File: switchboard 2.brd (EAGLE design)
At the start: 100 x 65 mm, 217 parts, among them IC1 MT8816AP, IC10 Z8F2480SO, IC11 LMV321M5, IC12 74HC595D, IC14 74LVC1G125DBV, IC15 74LVC1G125DBV, IC16 LM2940-9, IC17 PC817S OPTO, IC2 NE5532D, IC3 TC7660-SOIC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

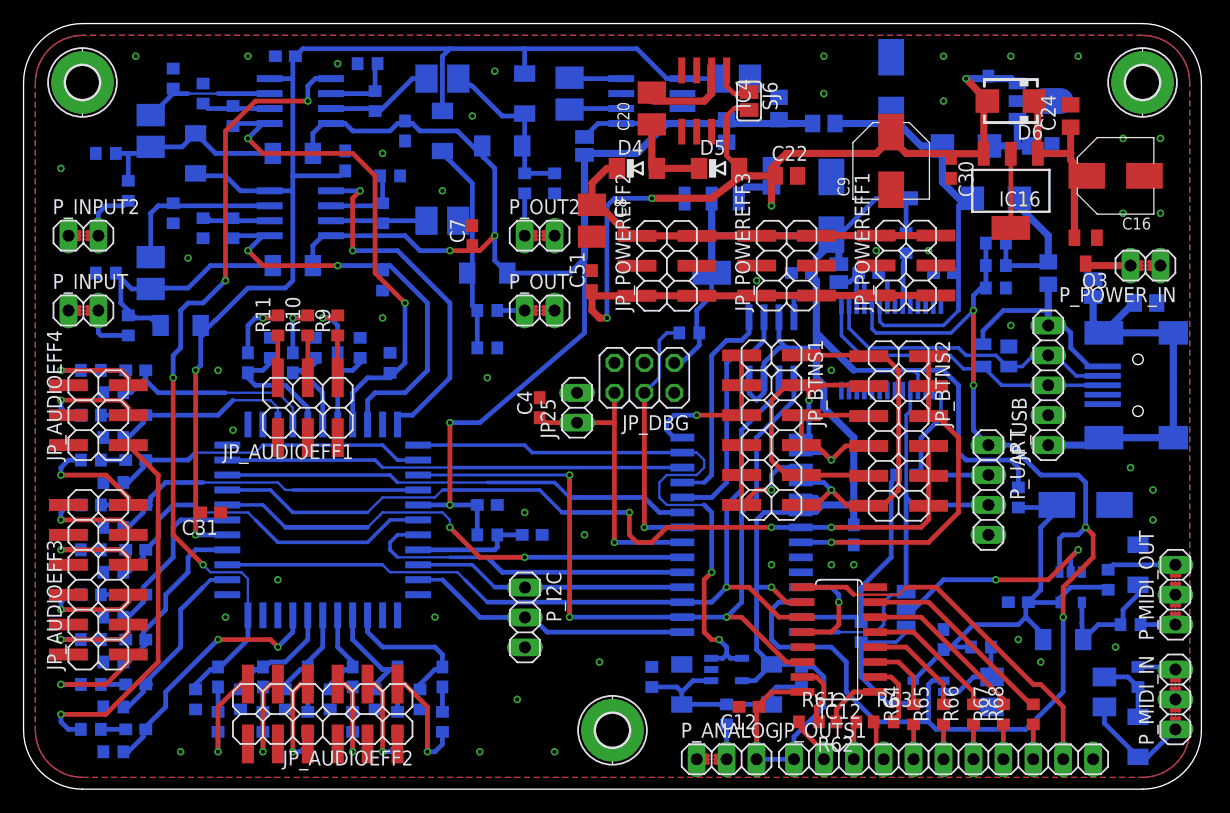
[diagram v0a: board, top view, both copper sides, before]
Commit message: Polarity inversion protection diode added to -5V. USB ESD protection connection changed from GND to USB shield. Layout development and changes to improve performance, considering current loops.
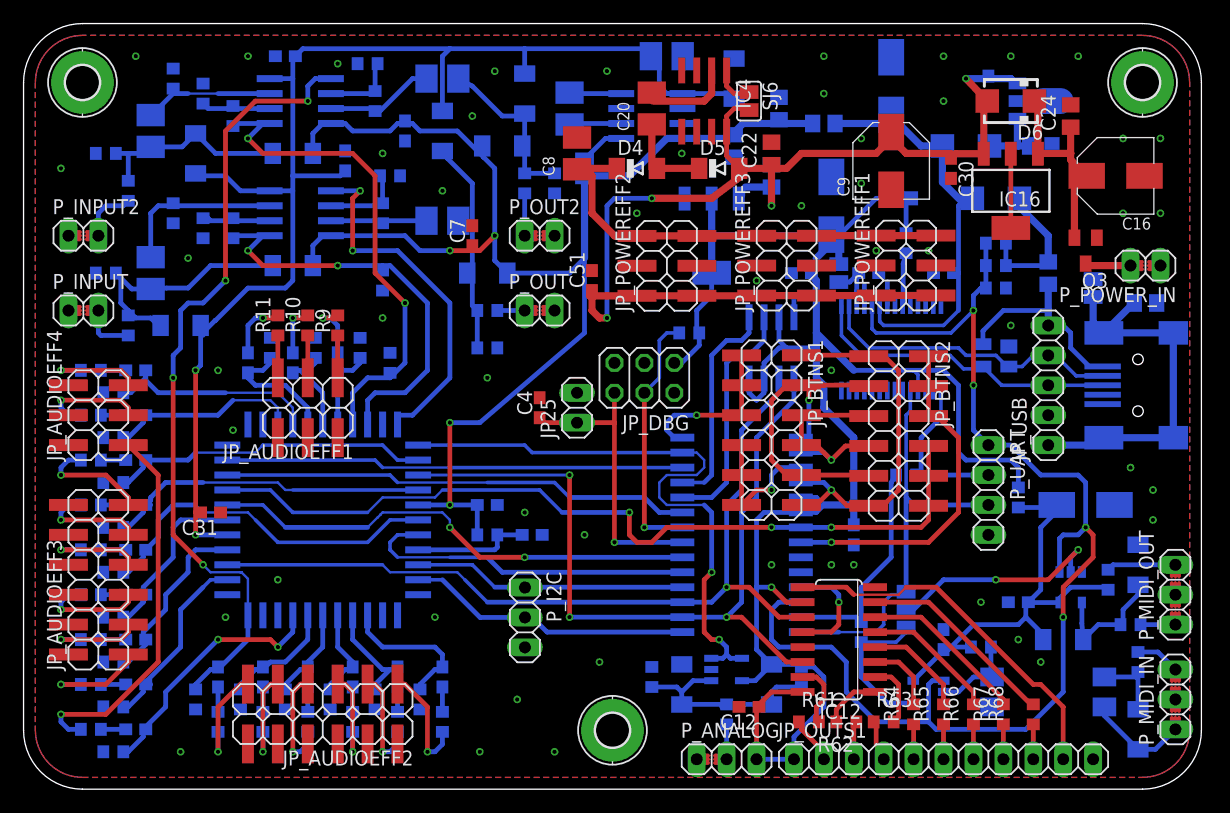
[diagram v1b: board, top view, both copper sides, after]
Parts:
- added D20: LL4148, diode:MINIMELF
- moved C19 6.02 mm to (54.6, 62.2)
- moved C8 5.85 mm to (47.0, 54.0), turned to 90 degrees
- moved C22 2.29 mm to (63.5, 54.0), turned to 90 degrees
- moved SJ1 1.91 mm to (47.6, 52.7)
- moved C25 1.42 mm to (60.3, 54.6)
- moved C5 1.27 mm to (46.4, 57.8)
- moved IC3 1.27 mm to (53.3, 57.1)
- moved R5 1.27 mm to (94.6, 10.8)
- moved D3 0.63 mm to (94.6, 5.08)
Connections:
- net -5V: now also D20.A
- net GND: now also D20.C, H1.B2,8, H2.B2,8, H3.B2,8; no longer D19.1
- net USB_SHLD: now also D19.1
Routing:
- net -5V: track 111.7 -> 115.9 mm
- net +18V: track 36.7 -> 40.6 mm
- net N$5: track 4.92 -> 3.85 mm
- net MIDI_IN2: track 11.1 -> 10.1 mm
- net MIDI_IN1: track 4.03 -> 4.86 mm
- net +9V: track 106.9 -> 107.6 mm
- net GND1: track 1.52 -> 2.16 mm
- net N$28: track 5.73 -> 6.27 mm
- net GND: vias 47 -> 53

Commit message: Final adjustments to the schematic and layout. Cap added close to the generic input opamp. RC filter against EMI added to the audio inputs. Bias resistors added to output opamps.
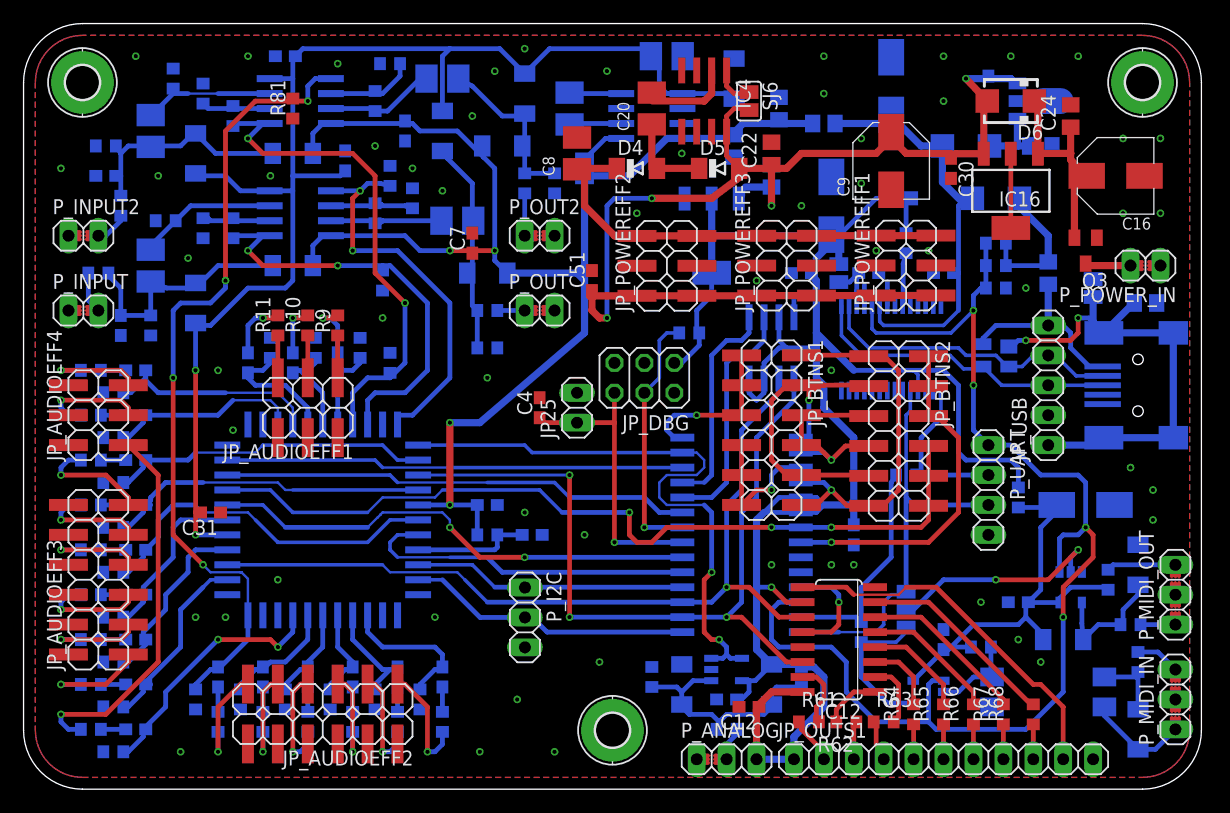
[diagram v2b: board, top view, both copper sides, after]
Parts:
- added C14: 100n, rcl:C0603
- added C58, C59: 100p, rcl:C0603
- added R81, R82: 1M, rcl:R0603
- R23, R25: value 1k -> 100
- moved R2 5.85 mm to (10.8, 39.4), turned to 90 degrees
- moved R4 5.12 mm to (6.35, 43.8), turned to 0 degrees
- moved R43 2.69 mm to (33.0, 50.2), turned to 270 degrees
- moved D1 2.29 mm to (14.6, 41.3), turned to 270 degrees
- moved R29 1.90 mm to (31.1, 61.6)
- moved R17 1.42 mm to (8.26, 49.5)
- moved R69 1.27 mm to (59.7, 5.08), turned to 180 degrees
- moved C10 1.27 mm to (36.8, 48.3)
- moved R3 0.90 mm to (12.1, 48.3), turned to 180 degrees
- moved C2 0.64 mm to (10.8, 44.5)
- moved C7 0.64 mm to (38.1, 46.4)
- moved R42 0.64 mm to (29.8, 48.9)
- moved R14 0.63 mm to (6.99, 54.6)
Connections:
- net +3V3: now also C14.1
- net GND: now also C14.2, C58.2, C59.2, R81.1, R82.1
- net N$4: now also C58.1
- net N$54: now also C59.1
- net SWOUT_1: now also R82.2
- net SWOUT_2-TO_EFF_7: now also R81.2
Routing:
- net USB_SHLD: track 32.9 -> 42.0 mm, vias 0 -> 2
- net +3V3: track 160.3 -> 166.2 mm
- net SWOUT_1: track 31.0 -> 33.8 mm
- net N$3: track 14.3 -> 12.0 mm
- net INPUT2: track 5.95 -> 3.92 mm
- net N$54: track 18.2 -> 20.0 mm
- net AD0: track 18.6 -> 20.3 mm
- net N$8: track 8.36 -> 10.0 mm
- net N$14: track 21.0 -> 19.5 mm
- net N$58: track 6.22 -> 7.72 mm
- net +5V_AN: track 122.0 -> 120.5 mm
- net INPUT1: track 5.30 -> 4.29 mm
- net SWOUT_2-TO_EFF_7: track 68.3 -> 69.3 mm
- net VIN_USB: track 17.7 -> 16.8 mm
- net N$7: track 6.89 -> 7.60 mm
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
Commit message: Final adjustments. Test points added to SPI and supplies. PTSK Engineering text added (in solder mask stop layer).
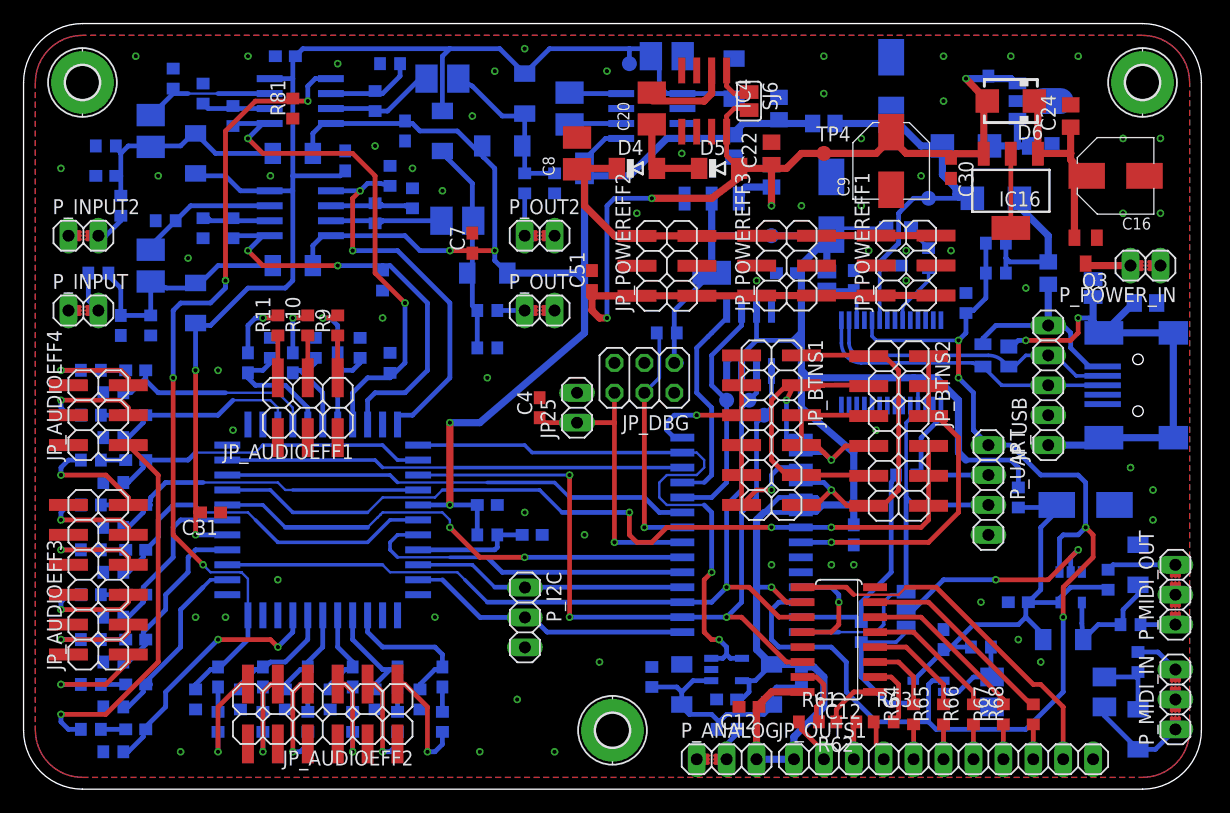
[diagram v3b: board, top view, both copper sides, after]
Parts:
- added TP1, TP2, TP3, TP4, TP5, TP6, TP7: TPB1,27, testpad:B1,27
- moved C29 4.49 mm to (73.7, 44.5), turned to 180 degrees
- moved R21 2.84 mm to (80.0, 41.3), turned to 90 degrees
- moved LED2 2.54 mm to (74.3, 47.6)
- moved R22 2.29 mm to (76.8, 45.1)
- moved IC8 2.01 mm to (61.6, 38.1)
- moved R55 1.91 mm to (54.6, 38.7)
- moved C33 1.42 mm to (70.5, 43.2), turned to 90 degrees
- moved C15 1.27 mm to (64.8, 43.8)
- moved IC5 1.27 mm to (73.7, 36.2)
- moved SJ4 1.20 mm to (68.2, 43.2)
- moved R20 0.64 mm to (82.5, 43.8)
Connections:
- net +3V3: now also TP6.TP
- net +5V: now also TP5.TP
- net +9V: now also TP4.TP
- net -5V: now also TP7.TP
- net MISO: now also TP1.TP
- net MOSI: now also TP2.TP
- net SCK: now also TP3.TP
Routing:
- net GND: track 17.8 -> 12.2 mm, vias 58 -> 61
- net BTN1: track 29.3 -> 31.2 mm
- net +5V: track 35.9 -> 34.1 mm
- net -5V: track 115.4 -> 117.2 mm
- net UART_TX: track 35.9 -> 34.7 mm
- net USB_TO_UART_RX: track 14.0 -> 12.7 mm
- net DBG: track 21.6 -> 20.4 mm
- net 5V_USB: track 12.2 -> 13.3 mm
- net +3V3: track 166.2 -> 167.1 mm
- net N$45: track 4.47 -> 5.33 mm
- net N$33: track 3.13 -> 2.31 mm
- net D-: track 25.9 -> 25.3 mm
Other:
- board text added: "2018"
- board text added: "ENGINEERING"
- board text added: "PTSK"

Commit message: Layout changes to improve manufacturability and EMC. RESET pin removed.
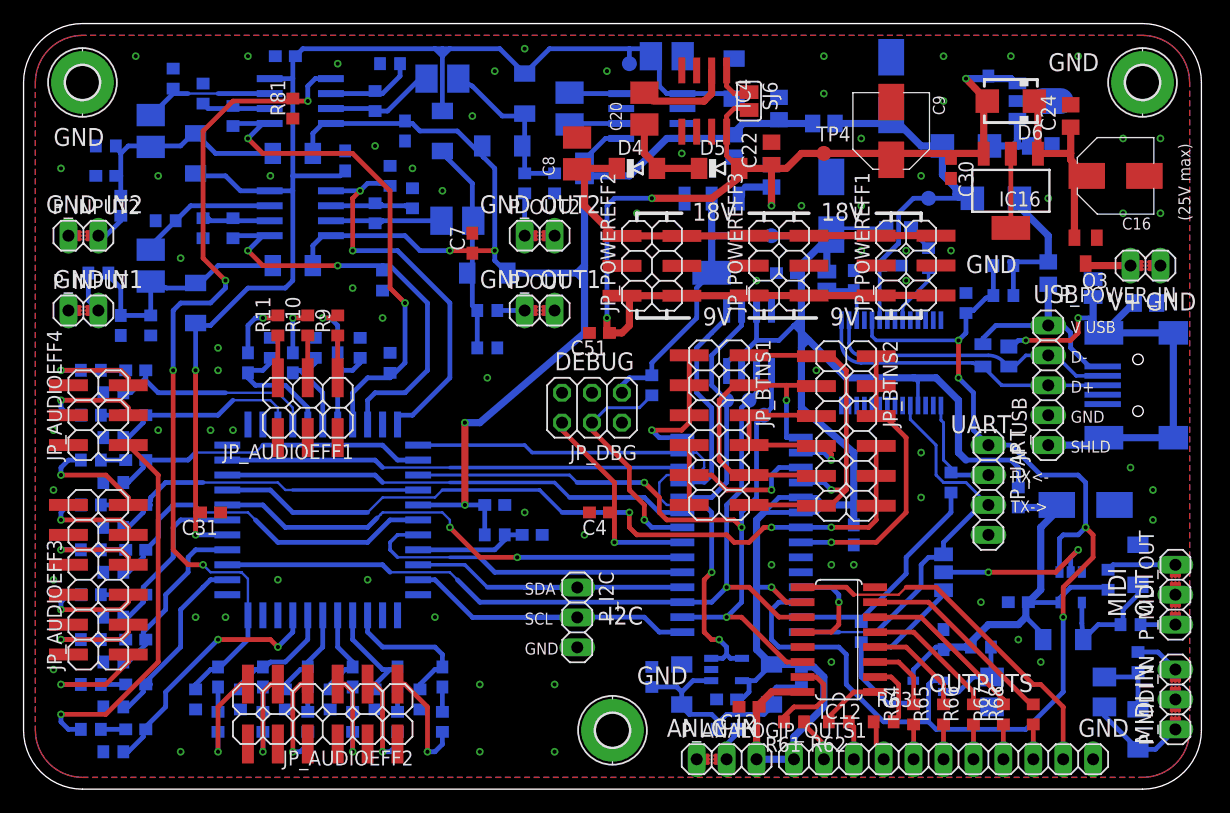
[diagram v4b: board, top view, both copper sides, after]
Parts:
- removed JP25: (no value), pinhead:1X02
- moved C4 10.2 mm to (48.9, 23.5), turned to 180 degrees
- moved JP_DBG 5.12 mm to (48.3, 32.4)
- moved R55 4.62 mm to (53.3, 34.3), turned to 270 degrees
- moved C51 4.49 mm to (48.9, 38.7), turned to 180 degrees
- moved SJ3 4.49 mm to (78.1, 18.4)
- moved P_I2C 4.45 mm to (47.0, 14.6)
- moved JP_BTNS1 4.44 mm to (60.3, 35.6)
- moved JP_BTNS2 4.44 mm to (71.1, 35.5)
- moved R71 3.86 mm to (78.7, 26.0), turned to 270 degrees
- moved C9 2.54 mm to (73.7, 55.9), turned to 270 degrees
- moved R20 2.01 mm to (83.2, 41.9)
- moved R54 2.01 mm to (83.2, 44.5)
- moved JP_POWEREFF2 1.27 mm to (52.1, 43.2)
- moved R61 1.27 mm to (65.4, 5.71), turned to 180 degrees
- moved C20 0.64 mm to (52.7, 57.8)
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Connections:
- net GND: no longer JP25.2
- net RST: no longer JP25.1
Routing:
- net C_SW1/SCL: track 24.3 -> 33.1 mm
- net +3V3: track 167.1 -> 174.0 mm
- net RST: track 25.0 -> 18.2 mm
- net BTN6/C_SW3: track 71.1 -> 66.3 mm
- net N$83: track 12.8 -> 17.5 mm
- net N$61: track 18.9 -> 14.4 mm
- net MOSI: track 68.8 -> 64.3 mm
- net BTN4: track 12.2 -> 16.6 mm
- net BTN5: track 29.2 -> 24.7 mm
- net C_SW4/SDA: track 24.5 -> 28.9 mm
- net BTN2: track 31.8 -> 36.0 mm
- net SWOUT_2-TO_EFF_7: track 69.3 -> 72.7 mm
- net USB_TO_UART_RX: track 12.7 -> 9.30 mm
- net BTN0: track 17.9 -> 21.1 mm
- net USB_DETECT: track 104.8 -> 101.5 mm
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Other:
- board text added: "(25V max)"
- board text added: "18V"
- board text added: "9V"
- board text added: "ANLG IN"
- board text added: "D+"
- board text added: "D-"
- board text added: "DEBUG"
- board text added: "GND"
- board text added: "I2C"
- board text added: "IN1"
- board text added: "IN2"
- board text added: "MIDI IN"
- board text added: "MIDI OUT"
- board text added: "OUT1"
- board text added: "OUT2"
- board text added: "OUTPUTS"
- board text added: "RX<-"
- board text added: "SCL"
- board text added: "SDA"
- board text added: "SHLD"
- board text added: "TX->"
- board text added: "UART"
- board text added: "USB"
- board text added: "V USB"
- board text added: "V+"

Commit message: Teardrops added to vias.
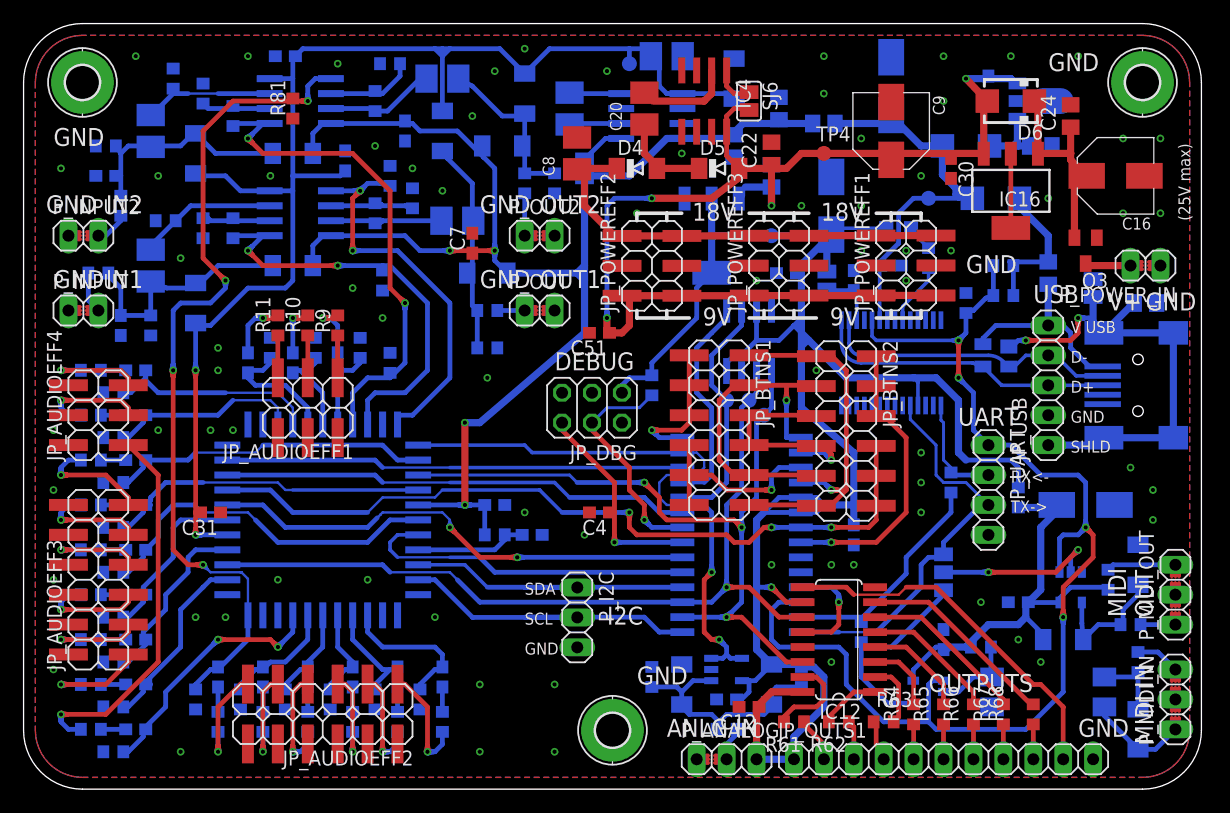
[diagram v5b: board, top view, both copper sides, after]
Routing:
- net USB_DETECT: track 101.5 -> 114.3 mm
- net SWOUT_2-TO_EFF_7: track 72.7 -> 83.0 mm
- net MOSI: track 64.3 -> 74.5 mm
- net +5V_AN: track 119.8 -> 128.7 mm
- net BTN6/C_SW3: track 66.3 -> 73.9 mm
- net SWOUT_1: track 33.8 -> 40.1 mm
- net C_SW2: track 41.9 -> 47.1 mm
- net FROM_EFF_9: track 21.7 -> 26.7 mm
- net SW_IN_2: track 43.2 -> 48.3 mm
- net SW_IN_1: track 37.0 -> 42.1 mm
- net CS_SWITCH/AD0: track 52.4 -> 57.5 mm
- net N$61: track 14.4 -> 19.4 mm
- net -5V: track 118.7 -> 123.8 mm
- net USB_SHLD: track 42.0 -> 47.1 mm
- net SCK: track 71.1 -> 74.9 mm
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
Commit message: Final adjustments. PLCC-44 and aluminum electrolytic cap packages updated.
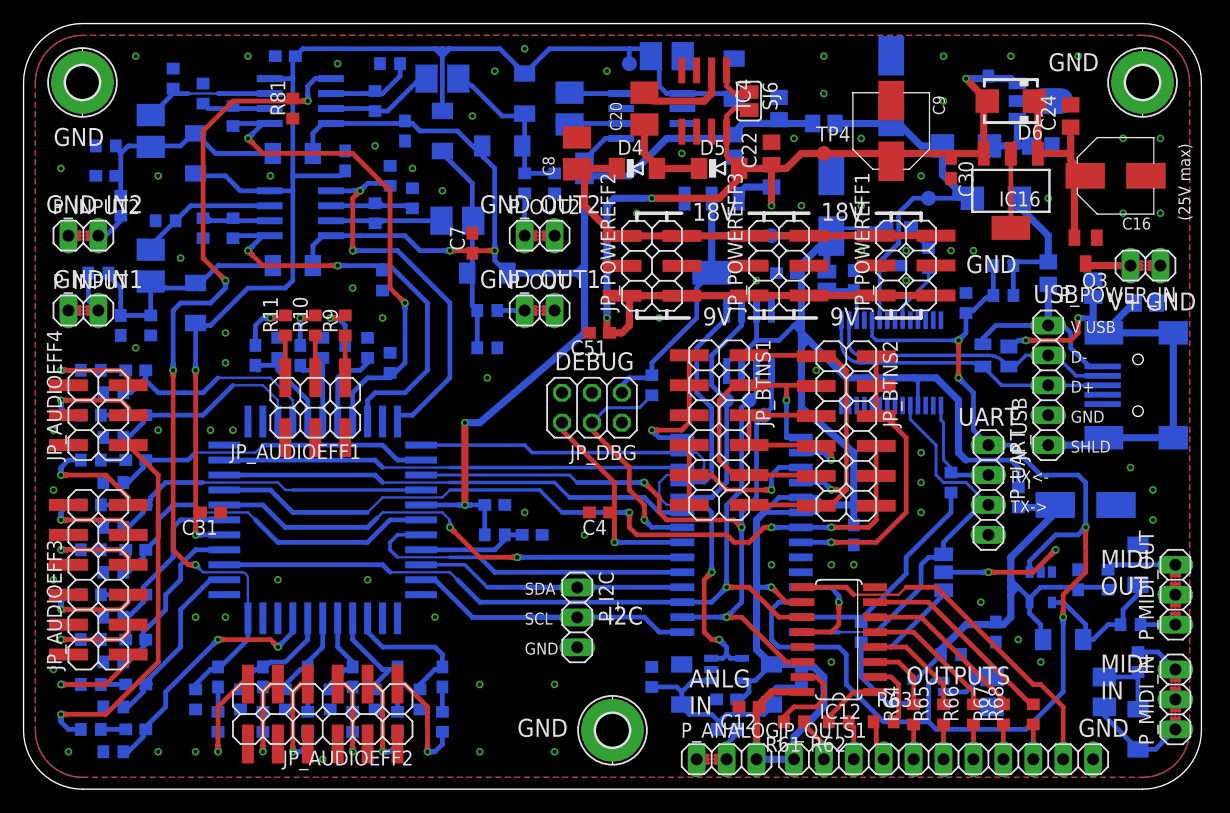
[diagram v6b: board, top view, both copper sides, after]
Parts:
- moved C13 5.43 mm to (89.5, 17.8), turned to 90 degrees
- moved C18 4.49 mm to (82.5, 13.3), turned to 270 degrees
- moved R6 2.62 mm to (78.7, 11.4)
- moved IC15 2.54 mm to (86.4, 17.1)
- moved C36 0.90 mm to (23.5, 36.8)
- moved C35 0.90 mm to (27.3, 36.8)
- moved C37 0.90 mm to (19.7, 36.8)
- moved JP_AUDIOEFF1 0.64 mm to (26.0, 31.1)
- moved R1 0.64 mm to (29.2, 37.5)
- moved R10 0.64 mm to (24.8, 39.4)
- moved R11 0.64 mm to (22.2, 39.4)
- moved R31 0.64 mm to (21.6, 37.5)
- moved R30 0.63 mm to (25.4, 37.5)
- moved R9 0.63 mm to (27.3, 39.4)
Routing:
- net 3V3_MIDI: track 38.9 -> 42.6 mm
- net N$100: track 7.95 -> 11.1 mm
- net N$2: track 10.9 -> 12.7 mm
- net N$61: track 19.4 -> 17.8 mm
- net FROM_EFF_11: track 18.2 -> 19.3 mm
- net FROM_EFF_10: track 16.4 -> 17.5 mm
- net FROM_EFF_1: track 7.33 -> 8.43 mm
- net USB_DETECT: track 114.3 -> 115.4 mm
- net N$17: track 7.75 -> 7.12 mm
- net N$16: track 6.86 -> 6.22 mm
- net N$15: track 7.75 -> 7.12 mm
- net FROM_EFF_3: track 10.7 -> 10.1 mm
- net GND: vias 74 -> 81
